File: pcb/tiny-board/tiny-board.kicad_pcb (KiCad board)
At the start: 2 copper layers, 100.3 x 99.7 mm, 44 parts, among them J1 USB_B, J2 EXPBUS1, J3 Serial, J6 UART1, SW1 RESET, SW2 NMI, SW3 SW_SPDT, U1 74AC14, U2 W65C02, U3 CD74HC688, U4 74AC10, U5 SST39SF040, U6 62256-55, U7 CD74HC688, U8 W65C51NxP, U9 MAX232, X1 14 MHz, Y1 1.8432 MHz

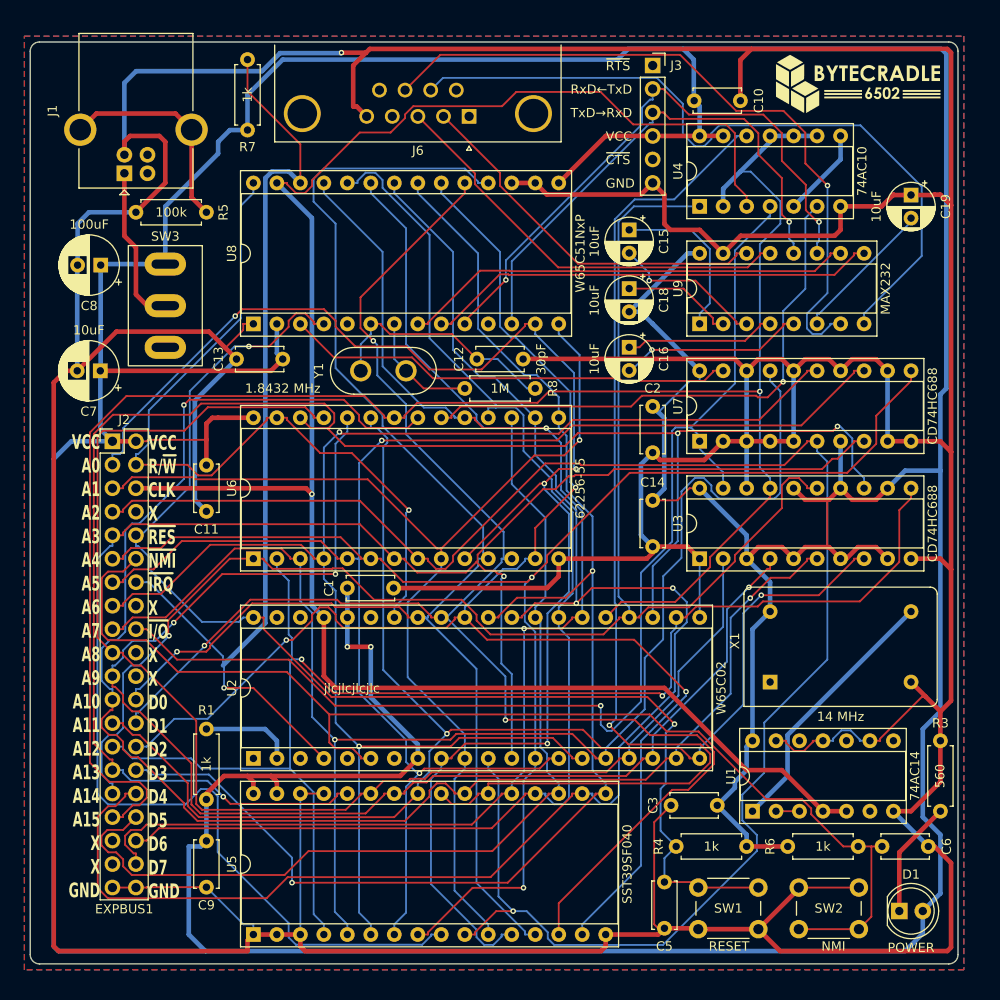
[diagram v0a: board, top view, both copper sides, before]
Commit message: Revising TINY board and creating test ROM for TINY board
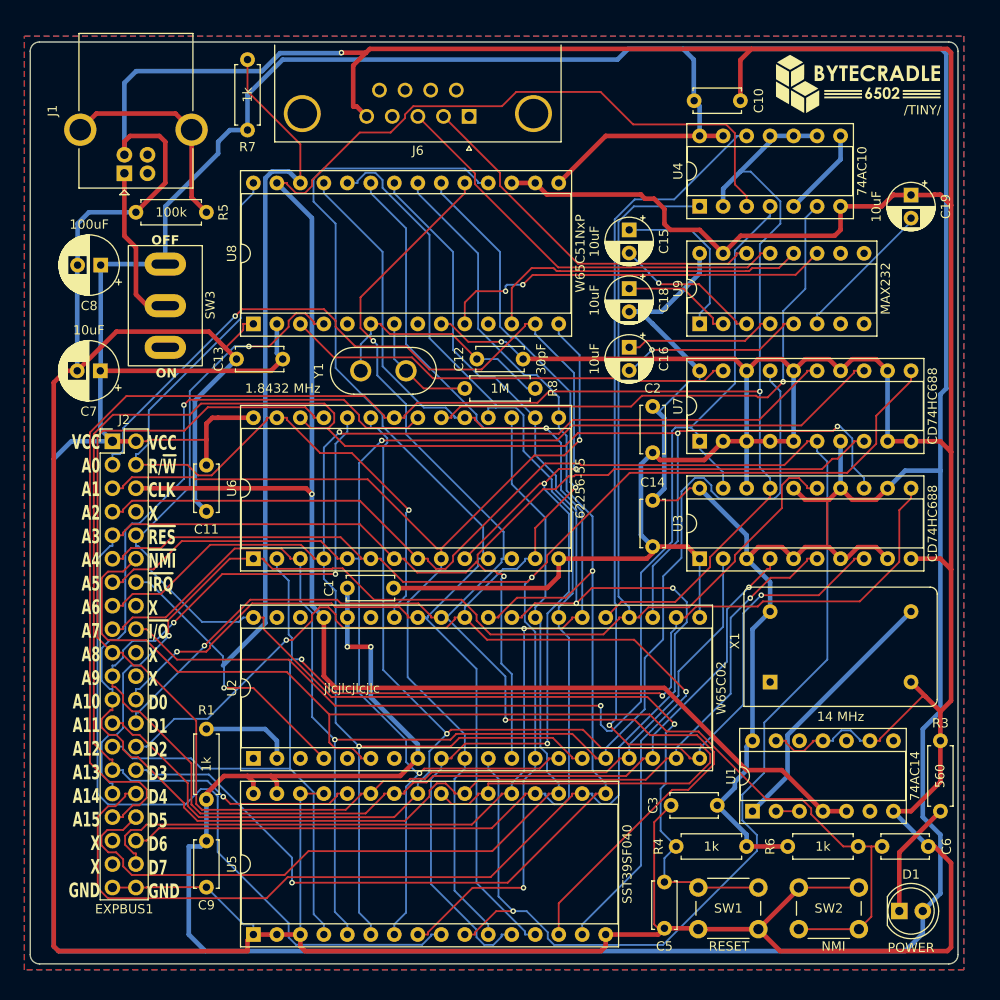
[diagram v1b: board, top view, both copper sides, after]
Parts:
- removed J3: Serial, Connector_PinSocket_2.54mm:PinSocket_1x06_P2.54mm_Vertical
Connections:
- J6 pad 7: Net-(U9-R2IN) -> unconnected-(J6-Pad7)
- J6 pad 8: Net-(U9-T2OUT) -> unconnected-(J6-Pad8)
- U8 pad 8: RTSD1 -> GND
- U8 pad 9: CTSD1 -> GND
- U9 pad 10: RTSD1 -> unconnected-(U9-T2IN-Pad10)
- U9 pad 7: Net-(U9-T2OUT) -> unconnected-(U9-T2OUT-Pad7)
- U9 pad 8: Net-(U9-R2IN) -> unconnected-(U9-R2IN-Pad8)
- U9 pad 9: CTSD1 -> unconnected-(U9-R2OUT-Pad9)
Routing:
- net Net-(U9-R2IN): track 80.1 -> 0.00 mm
- net Net-(U9-T2OUT): track 75.9 -> 0.00 mm, vias 1 -> 0
- net CTSD1: track 49.1 -> 0.00 mm
- net RTSD1: track 49.1 -> 0.00 mm
- net TxD1: track 64.8 -> 42.9 mm
- net RxD1: track 56.3 -> 36.2 mm, vias 1 -> 0
- net GND: track 766.2 -> 774.7 mm, vias 1 -> 2
- net VCC: track 667.3 -> 668.6 mm
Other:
- board text added: "/TINY/"
- board text added: "OFF"
- board text added: "ON"
- board text removed: "GND"
- board text removed: "RxD←TxD"
- board text removed: "TxD→RxD"
- board text removed: "VCC"
- board text removed: "~{CTS}"
- board text removed: "~{RTS}"

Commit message: Revising TINY board and writing CUPL
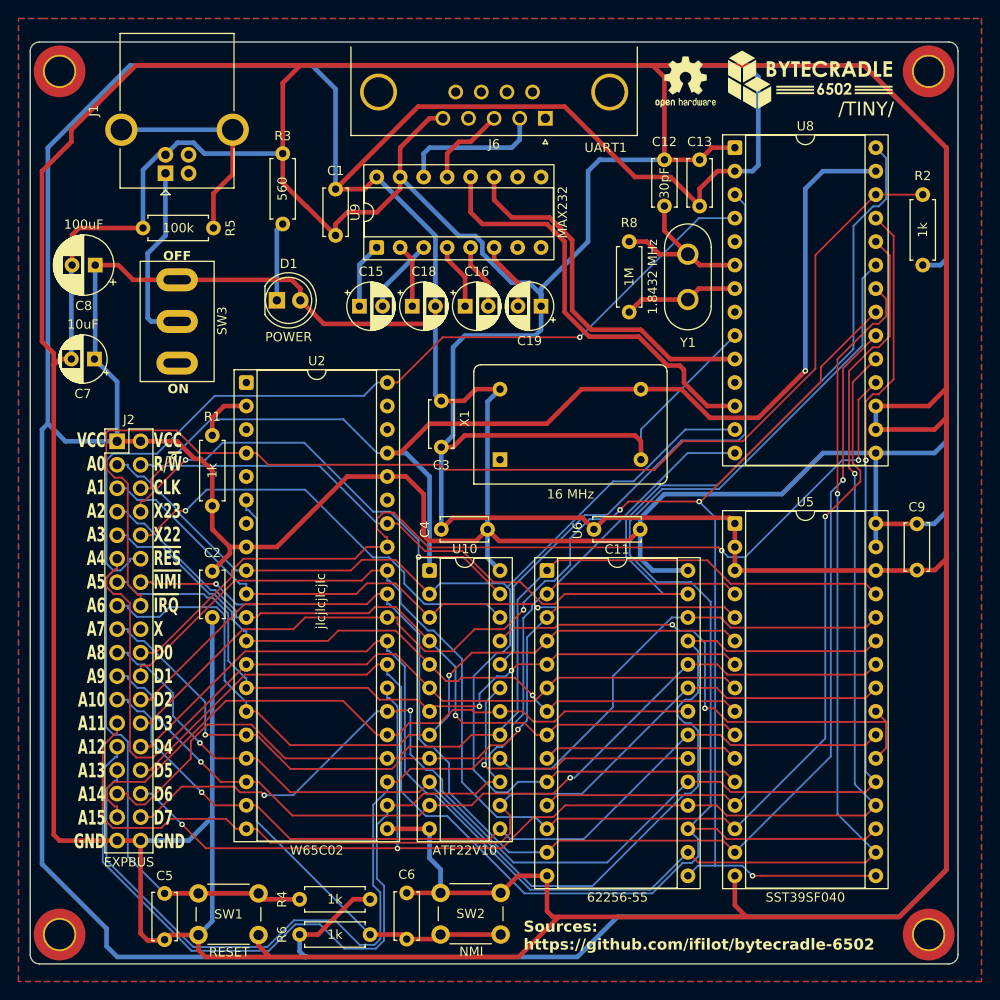
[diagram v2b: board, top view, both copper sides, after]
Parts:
- removed C10, C14: 100nF, Capacitor_THT:C_Disc_D5.0mm_W2.5mm_P5.00mm
- removed R7: 1k, Resistor_THT:R_Axial_DIN0207_L6.3mm_D2.5mm_P7.62mm_Horizontal
- removed U1: 74AC14, Package_DIP:DIP-14_W7.62mm_Socket
- removed U3, U7: CD74HC688, Package_DIP:DIP-20_W7.62mm_Socket
- removed U4: 74AC10, Package_DIP:DIP-14_W7.62mm_Socket
- added C4: 100nF, Capacitor_THT:C_Disc_D5.0mm_W2.5mm_P5.00mm, F.Cu at (99.0, 103.5)
- added H1: MountingHole, MountingHole:MountingHole_3.2mm_M3_DIN965_Pad_TopOnly, F.Cu at (52.7, 54.0)
- added H2: MountingHole, MountingHole:MountingHole_3.2mm_M3_DIN965_Pad_TopOnly, F.Cu at (52.7, 147.3)
- added H3: MountingHole, MountingHole:MountingHole_3.2mm_M3_DIN965_Pad_TopOnly, F.Cu at (146.7, 54.0)
- added H4: MountingHole, MountingHole:MountingHole_3.2mm_M3_DIN965_Pad_TopOnly, F.Cu at (146.7, 147.3)
- added R2: 1k, Resistor_THT:R_Axial_DIN0207_L6.3mm_D2.5mm_P7.62mm_Horizontal, F.Cu at (146.1, 67.3)
- added REF**: OSHW-Logo2_7.3x6mm_SilkScreen, Symbol:OSHW-Logo2_7.3x6mm_SilkScreen, F.Cu at (120.4, 55.1)
- added U10: ATF22V10, Package_DIP:DIP-24_W7.62mm_Socket, F.Cu at (92.7, 108.0)
- C7: footprint Capacitor_THT:CP_Radial_D6.3mm_P2.50mm -> Capacitor_THT:CP_Radial_D5.0mm_P2.50mm
- J2: value EXPBUS1 -> EXPBUS; footprint Connector_PinHeader_2.54mm:PinHeader_2x20_P2.54mm_Vertical -> Connector_PinHeader_2.54mm:PinHeader_2x18_P2.54mm_Vertical
- J6: footprint Connector_Dsub:DSUB-9_Male_Horizontal_P2.77x2.84mm_EdgePinOffset4.94mm_Housed_MountingHolesOffset7.48mm -> Connector_Dsub:DSUB-9_Pins_Horizontal_P2.77x2.84mm_EdgePinOffset4.94mm_Housed_MountingHolesOffset4.94mm
- X1: value 14 MHz -> 16 MHz
- moved R3 95.3 mm to (76.8, 62.9)
- moved D1 94.3 mm to (76.2, 78.7)
- moved C9 84.1 mm to (145.4, 102.9)
- moved U5 68.5 mm to (125.7, 102.9), turned to 0 degrees
- moved U8 55.4 mm to (125.7, 62.2), turned to 0 degrees
- moved C5 54.1 mm to (64.1, 142.9)
- moved SW1 54.1 mm to (74.2, 147.4)
- moved R6 53.6 mm to (86.3, 147.3)
- moved C3 52.9 mm to (94.0, 89.6), turned to -90 degrees
- moved C6 52.4 mm to (90.2, 147.8), turned to 90 degrees
- moved C2 50.8 mm to (69.2, 108.0)
- moved C13 48.0 mm to (121.9, 68.5), turned to 90 degrees
- moved C11 47.4 mm to (115.5, 103.5), turned to 180 degrees
- moved C1 43.2 mm to (82.5, 66.7), turned to -90 degrees
- moved C19 41.8 mm to (104.8, 79.4), turned to 180 degrees
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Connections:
- net Net-(U5-CE) renamed ~{ROMCS}
- J2 pad 10: ~{RES} -> ATF22IO22
- J2 pad 12: ~{NMI} -> ~{RES}
- J2 pad 14: ~{IRQC51_1} -> ~{NMI}
- J2 pad 16: unconnected-(J2-Pin_16-Pad16) -> ~{IRQ}
- J2 pad 18: ~{I/O} -> unconnected-(J2-Pin_18-Pad18)
- J2 pad 20: unconnected-(J2-Pin_20-Pad20) -> D0
- J2 pad 22: unconnected-(J2-Pin_22-Pad22) -> D1
- J2 pad 24: D0 -> D2
- J2 pad 26: D1 -> D3
- J2 pad 28: D2 -> D4
- J2 pad 30: D3 -> D5
- J2 pad 32: D4 -> D6
- J2 pad 34: D5 -> D7
- J2 pad 35: unconnected-(J2-Pin_35-Pad35) -> GND
- J2 pad 36: D6 -> GND
- J2 pad 8: unconnected-(J2-Pin_8-Pad8) -> ATF22IO23
- U2 pad 4: ~{IRQC51_1} -> ~{IRQ}
- U5 pad 29: GND -> A14
- U6 pad 20: Net-(U6-~{CS}) -> ~{RAMCS}
- U8 pad 26: ~{IRQC51_1} -> ~{IRQ}
- U8 pad 3: Net-(U7-P=R) -> ~{ACIACS}
- U8 pad 8: GND -> unconnected-(U8-~{RTS}-Pad8)
- X1 pad 8: Net-(X1-OUT) -> CLK
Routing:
- net ~{IRQ}: track 0.00 -> 130.5 mm
- net ~{I/O}: track 130.1 -> 0.00 mm, vias 1 -> 0
- net A15: track 202.9 -> 74.2 mm, vias 1 -> 0
- net A3: track 193.5 -> 78.2 mm
- net A2: track 192.1 -> 82.3 mm
- net ~{IRQC51_1}: track 105.1 -> 0.00 mm, vias 1 -> 0
- net A5: track 159.2 -> 80.2 mm
- net A6: track 163.7 -> 87.0 mm, vias 2 -> 1
- net CLK: track 202.8 -> 127.2 mm, vias 1 -> 2
- net A10: track 169.4 -> 96.4 mm, vias 2 -> 1
- net VCC: track 668.6 -> 737.9 mm, vias 2 -> 0
- net A7: track 156.8 -> 88.3 mm, vias 1 -> 2
- net ~{ACIACS}: track 0.00 -> 67.2 mm
- net ~{ROMCS}: track 118.4 -> 56.9 mm, vias 1 -> 2
- net Net-(U6-~{CS}): track 59.4 -> 0.00 mm, vias 1 -> 0
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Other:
- board text added: "Sources: https://github.com/ifilot/bytecradle-6502"
- board text added: "VCC A0 A1 A2 A3 A4 A5 A6 A7 A8 A9 A10 A11 A12 A13 A14 A15 GND"
- board text added: "VCC R/~{W} CLK X23 X22 ~{RES} ~{NMI} ~{IRQ} X D0 D1 D2 D3 D4 D5 D6 D7 GND"
- board text removed: "VCC A0 A1 A2 A3 A4 A5 A6 A7 A8 A9 A10 A11 A12 A13 A14 A15 X X GND"
- board text removed: "VCC R/~{W} CLK X ~{RES} ~{NMI} ~{IRQ} X ~{I/O} X X D0 D1 D2 D3 D4 D5 D6 D7 GND"

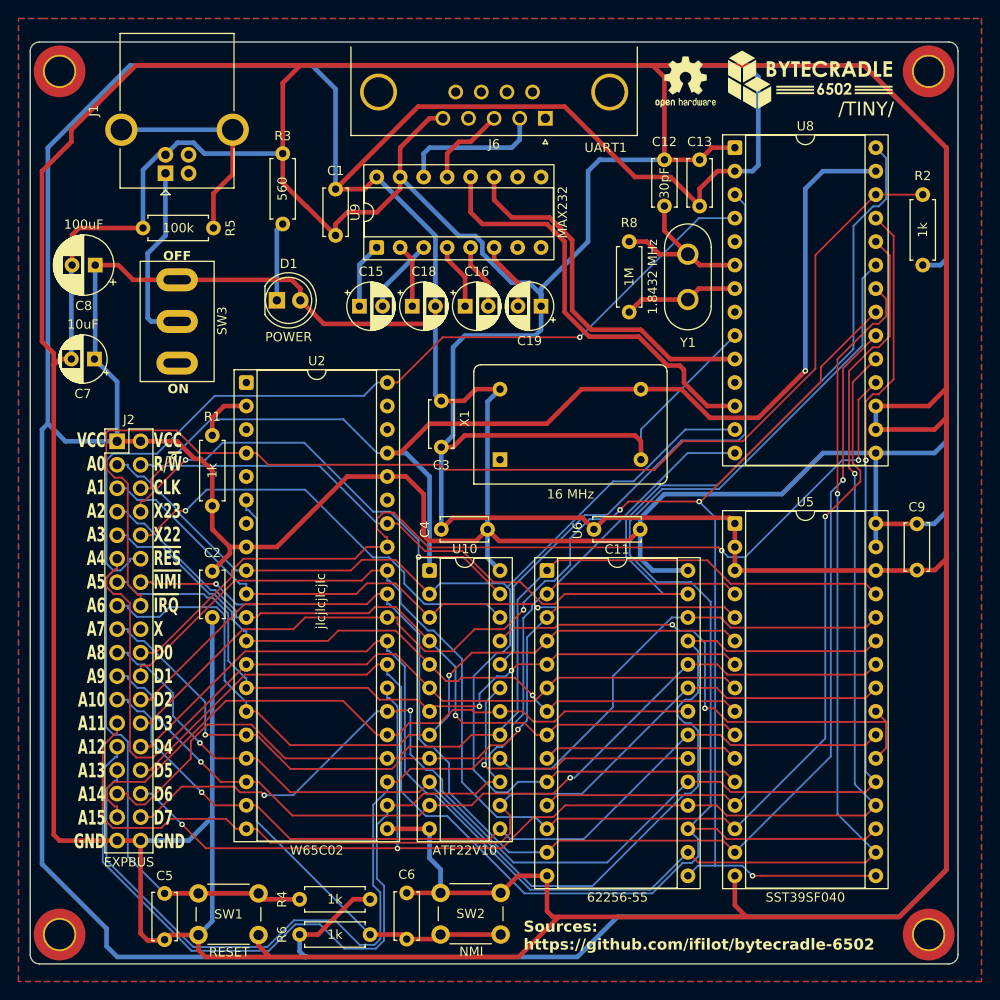
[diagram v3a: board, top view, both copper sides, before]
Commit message: Revising board and integrating DS1813
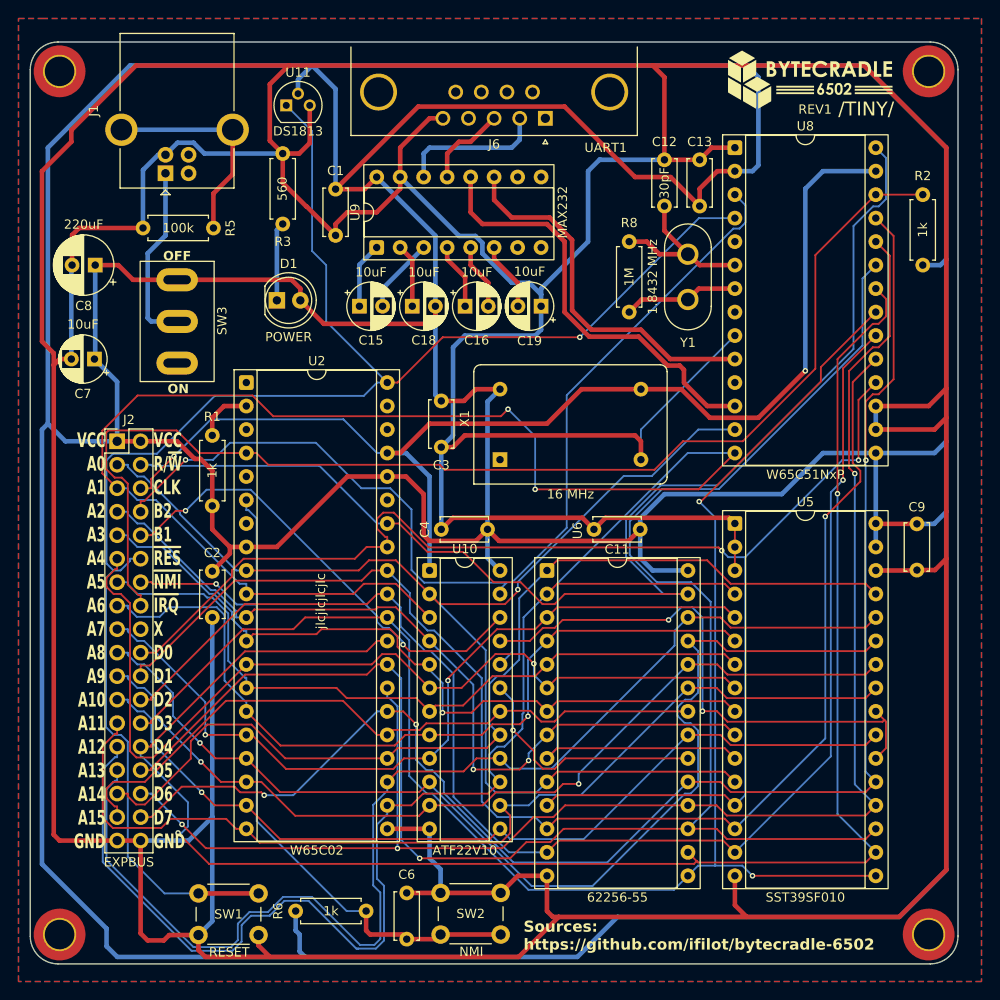
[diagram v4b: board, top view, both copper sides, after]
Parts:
- removed C5: 100nF, Capacitor_THT:C_Disc_D5.0mm_W2.5mm_P5.00mm
- removed R4: 1k, Resistor_THT:R_Axial_DIN0207_L6.3mm_D2.5mm_P7.62mm_Horizontal
- removed REF**: OSHW-Logo2_7.3x6mm_SilkScreen, Symbol:OSHW-Logo2_7.3x6mm_SilkScreen
- added U11: DS1813, Package_TO_SOT_THT:TO-92, F.Cu at (77.2, 57.7)
- C8: value 100uF -> 220uF
- U5: value SST39SF040 -> SST39SF010
- moved R6 2.58 mm to (85.9, 144.8)
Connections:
- net ATF22IO22 renamed B1
- net ATF22IO23 renamed B2
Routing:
- net A1: track 121.6 -> 193.6 mm, vias 1 -> 2
- net ~{RES}: track 147.8 -> 177.6 mm
- net D4: track 171.0 -> 188.3 mm, vias 1 -> 2
- net D3: track 165.9 -> 175.4 mm, vias 4 -> 2
- net GND: track 766.9 -> 758.4 mm
- net A2: track 82.3 -> 88.1 mm, vias 1 -> 2
- net ~{RAMCS}: track 31.7 -> 26.8 mm
- net ~{ACIACS}: track 67.2 -> 62.7 mm
- net B2: track 50.5 -> 55.0 mm, vias 2 -> 1
- net A3: track 78.2 -> 81.8 mm
- net D5: track 191.4 -> 187.9 mm, vias 0 -> 1
- net ~{ROMCS}: track 56.9 -> 60.2 mm
- net A12: track 124.1 -> 127.3 mm
- net VCC: track 737.9 -> 735.0 mm
- net B1: track 47.3 -> 50.2 mm, vias 1 -> 2
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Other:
- outline, holes or cut-outs redrawn
- board text added: "REV1"
- board text added: "VCC R/~{W} CLK B2 B1 ~{RES} ~{NMI} ~{IRQ} X D0 D1 D2 D3 D4 D5 D6 D7 GND"
- board text removed: "VCC R/~{W} CLK X23 X22 ~{RES} ~{NMI} ~{IRQ} X D0 D1 D2 D3 D4 D5 D6 D7 GND"

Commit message: Expanding README.md
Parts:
- added G002: OSHW-Logo2_7.3x6mm_SilkScreen, Symbol:OSHW-Logo2_7.3x6mm_SilkScreen, F.Cu at (120.4, 55.4)

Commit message: Revising tinyboard (REV2) and adding daughterboard with LEDs
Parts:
- J2: value EXPBUS -> SYSTEM BUS; footprint Connector_PinHeader_2.54mm:PinHeader_2x18_P2.54mm_Vertical -> Connector_PinHeader_2.54mm:PinHeader_2x20_P2.54mm_Vertical
- moved J2 2.54 mm to (58.9, 91.4)
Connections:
- J2 pad 18: unconnected-(J2-Pin_18-Pad18) -> ~{ROMCS}
- J2 pad 20: D0 -> ~{ACIACS}
- J2 pad 22: D1 -> ~{RAMCS}
- J2 pad 24: D2 -> D0
- J2 pad 26: D3 -> D1
- J2 pad 28: D4 -> D2
- J2 pad 30: D5 -> D3
- J2 pad 32: D6 -> D4
- J2 pad 34: D7 -> D5
- J2 pad 35: GND -> TxD1
- J2 pad 36: GND -> D6
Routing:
- net TxD1: track 40.1 -> 152.0 mm, vias 0 -> 1
- net RxD1: track 46.3 -> 151.2 mm
- net ~{RAMCS}: track 26.8 -> 118.1 mm, vias 1 -> 2
- net ~{ROMCS}: track 60.2 -> 117.2 mm, vias 2 -> 3
- net ~{ACIACS}: track 62.7 -> 106.1 mm, vias 0 -> 1
- net A1: track 193.6 -> 156.4 mm
- net A13: track 130.5 -> 94.9 mm, vias 0 -> 1
- net A12: track 127.3 -> 96.6 mm, vias 0 -> 2
- net VCC: track 735.0 -> 711.3 mm
- net A4: track 99.4 -> 81.4 mm
- net ~{IRQ}: track 130.5 -> 118.7 mm
- net D7: track 163.1 -> 172.1 mm
- net B2: track 55.0 -> 46.5 mm, vias 1 -> 3
- net GND: track 758.4 -> 750.0 mm
- net D4: track 188.3 -> 181.7 mm, vias 2 -> 3
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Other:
- board text added: "REV2"
- board text added: "VCC A0 A1 A2 A3 A4 A5 A6 A7 A8 A9 A10 A11 A12 A13 A14 A15 TxD RxD GND"
- board text added: "VCC R/~{W} CLK B2 B1 ~{RES} ~{NMI} ~{IRQ} ~{ROM} ~{ACIA} ~{RAM} D0 D1 D2 D3 D4 D5 D6 D7 GND"
- board text removed: "REV1"
- board text removed: "VCC A0 A1 A2 A3 A4 A5 A6 A7 A8 A9 A10 A11 A12 A13 A14 A15 GND"
- board text removed: "VCC R/~{W} CLK B2 B1 ~{RES} ~{NMI} ~{IRQ} X D0 D1 D2 D3 D4 D5 D6 D7 GND"

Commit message: Making small changes to tiny board and updating documentation
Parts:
- moved C13 2.41 mm to (102.4, 79.4), turned to 0 degrees
- renumbered C2 to C1, C1 to C10, C12 to C11, C18 to C12, C19 to C13, C16 to C14, C7 to C2, C8 to C4, C9 to C5, C4 to C7, C11 to C8, C13 to C9, J6 to J2, J2 to J3, R2 to R1, R5 to R2, R1 to R3, R6 to R4, R8 to R5, R3 to R6, SW3 to SW1, SW1 to SW2, SW2 to SW3, U2 to U1, U5 to U2, U11 to U3, U6 to U4, U10 to U5, U8 to U6, U9 to U7
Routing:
- net GND: track 750.0 -> 747.7 mm
- net Net-(U7-VS-): track 7.42 -> 8.49 mm
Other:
- board text added: "REV3"
- board text removed: "REV2"
